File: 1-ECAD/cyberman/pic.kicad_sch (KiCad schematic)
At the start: 0 parts

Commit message: add expander io and pic
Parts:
- added C50: 100nF, symbol Device:C
- added C51: 10nF, symbol Device:C
- added R34: 100R, symbol Device:R
- added R35: 10k, symbol Device:R
- added TP5, TP6: TestPoint, symbol Connector:TestPoint
- added U19: PIC16F13115T-I/SN, symbol 0_mcu_microchip:PIC16F13115T-I/SN
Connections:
- new net: R34.1, U19.4 (RA3)
- new net: C51.1, R34.2, R35.1
- new net +3V3: C50.1, R35.2, U19.1 (VDD)
- new net GND: C50.2, C51.2, U19.8 (VSS)
- new net ICSPCLK: TP6.1, U19.6 (RA1)
- new net ICSPDAT: TP5.1, U19.7 (RA0)

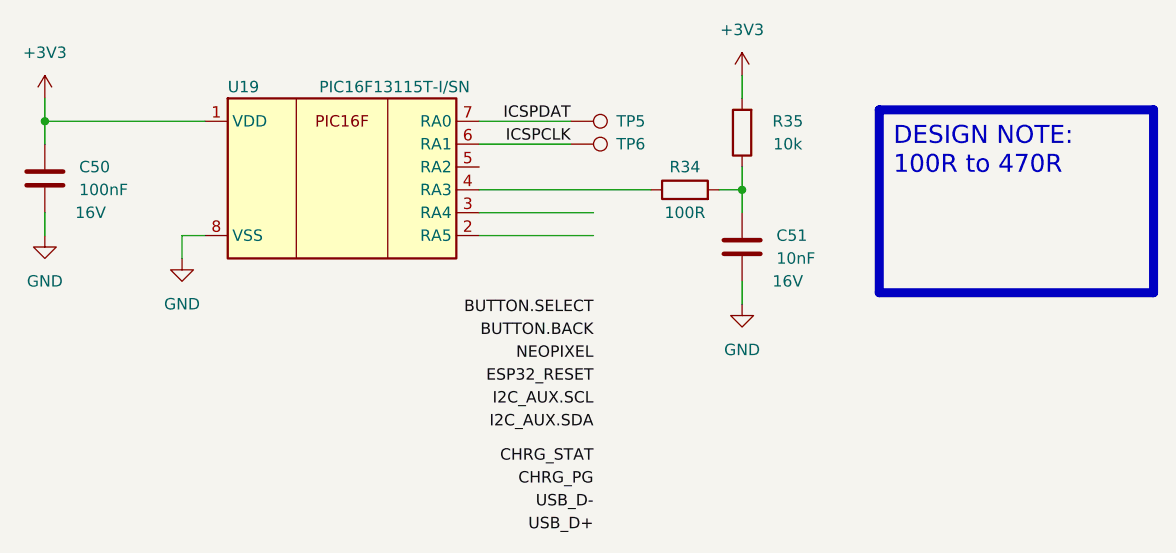
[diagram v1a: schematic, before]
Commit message: new changes
close display page and peripheral schematic
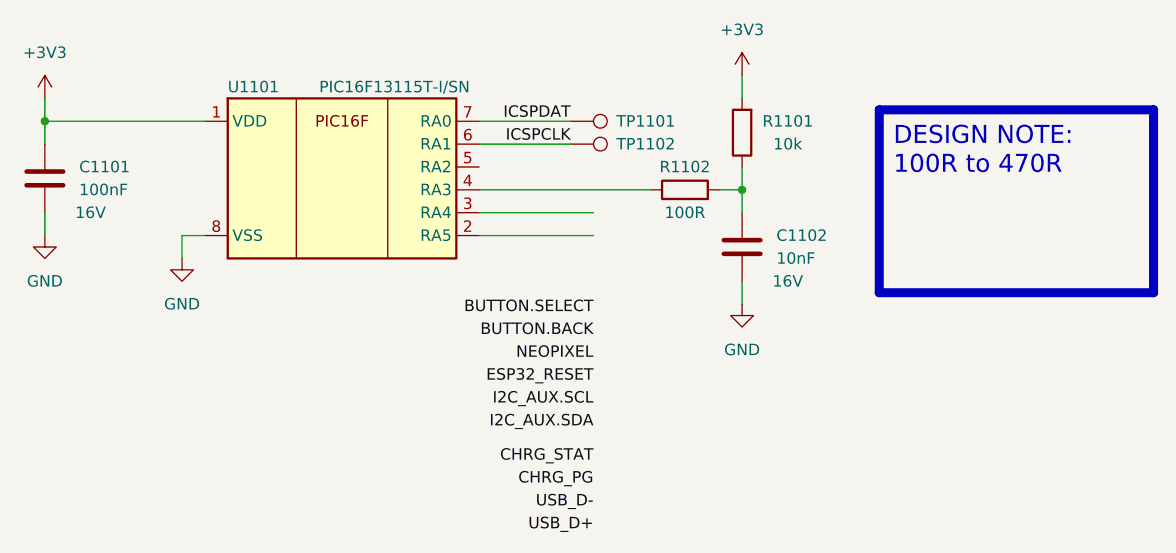
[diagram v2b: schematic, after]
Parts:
- renumbered C50 to C1101, C51 to C1102, R35 to R1101, R34 to R1102, TP5 to TP1101, TP6 to TP1102, U19 to U1101
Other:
- company: (none) -> kode.
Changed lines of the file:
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@@
 	(generator_version "8.0")
 	(paper "A4")
+	(title_block
+		(date "2024-12-11")
+		(rev "1.0")
+		(company "kode.")
+	)
 	(junction
 		(at 106.68 40.64)
@@
 		(dnp no)
 		(fields_autoplaced yes)
-		(property "Reference" "#PWR0126"
+		(property "Reference" "#PWR01105"
 			(at 184.15 67.31 0)
 			(effects
@@
 			(project "cyberman"
 				(path "/0650c7a8-acba-429c-9f8e-eec0baf0bc1c/fede4c36-00cc-4d3d-b71c-5243ba232202/9dd041dd-a789-48b0-a1c9-db40d4b09215"
-					(reference "#PWR0126")
+					(reference "#PWR01105")
 					(unit 1)
 				)
@@
 		(on_board yes)
 		(dnp no)
-		(property "Reference" "R34"
+		(property "Reference" "R1102"
 			(at 177.8 45.72 90)
 			(effects
@@
 			(project ""
 				(path "/0650c7a8-acba-429c-9f8e-eec0baf0bc1c/fede4c36-00cc-4d3d-b71c-5243ba232202/9dd041dd-a789-48b0-a1c9-db40d4b09215"
-					(reference "R34")
+					(reference "R1102")
 					(unit 1)
 				)
@@
 		(dnp no)
 		(fields_autoplaced yes)
-		(property "Reference" "#PWR0124"
+		(property "Reference" "#PWR01102"
 			(at 106.68 41.91 0)
 			(effects
@@
 			(project ""
 				(path "/0650c7a8-acba-429c-9f8e-eec0baf0bc1c/fede4c36-00cc-4d3d-b71c-5243ba232202/9dd041dd-a789-48b0-a1c9-db40d4b09215"
-					(reference "#PWR0124")
+					(reference "#PWR01102")
 					(unit 1)
 				)
@@
 		(on_board yes)
 		(dnp no)
-		(property "Reference" "TP5"
+		(property "Reference" "TP1101"
 			(at 170.18 40.64 90)
 			(effects
@@
 			(project ""
 				(path "/0650c7a8-acba-429c-9f8e-eec0baf0bc1c/fede4c36-00cc-4d3d-b71c-5243ba232202/9dd041dd-a789-48b0-a1c9-db40d4b09215"
-					(reference "TP5")
+					(reference "TP1101")
 					(unit 1)
 				)
@@
 		(dnp no)
 		(fields_autoplaced yes)
-		(property "Reference" "U19"
+		(property "Reference" "U1101"
 			(at 127 36.83 0)
 			(do_not_autoplace yes)
@@
 			(project ""
 				(path "/0650c7a8-acba-429c-9f8e-eec0baf0bc1c/fede4c36-00cc-4d3d-b71c-5243ba232202/9dd041dd-a789-48b0-a1c9-db40d4b09215"
-					(reference "U19")
+					(reference "U1101")
 					(unit 1)
 				)
@@
 		(on_board yes)
 		(dnp no)
-		(property "Reference" "C50"
+		(property "Reference" "C1101"
 			(at 110.49 45.72 0)
 			(effects
@@
 			(project ""
 				(path "/0650c7a8-acba-429c-9f8e-eec0baf0bc1c/fede4c36-00cc-4d3d-b71c-5243ba232202/9dd041dd-a789-48b0-a1c9-db40d4b09215"
-					(reference "C50")
+					(reference "C1101")
 					(unit 1)
 				)
@@
 		(dnp no)
 		(fields_autoplaced yes)
-		(property "Reference" "#PWR0122"
+		(property "Reference" "#PWR01104"
 			(at 121.92 62.23 0)
 			(effects
@@
 			(project ""
 				(path "/0650c7a8-acba-429c-9f8e-eec0baf0bc1c/fede4c36-00cc-4d3d-b71c-5243ba232202/9dd041dd-a789-48b0-a1c9-db40d4b09215"
-					(reference "#PWR0122")
+					(reference "#PWR01104")
 					(unit 1)
 				)
@@
 		(on_board yes)
 		(dnp no)
-		(property "Reference" "C51"
+		(property "Reference" "C1102"
 			(at 187.96 53.34 0)
 			(effects
@@
 			(project "cyberman"
 				(path "/0650c7a8-acba-429c-9f8e-eec0baf0bc1c/fede4c36-00cc-4d3d-b71c-5243ba232202/9dd041dd-a789-48b0-a1c9-db40d4b09215"
-					(reference "C51")
+					(reference "C1102")
 					(unit 1)
 				)
@@
 		(on_board yes)
 		(dnp no)
-		(property "Reference" "R35"
+		(property "Reference" "R1101"
 			(at 189.23 40.64 0)
 			(effects
@@
 			(project "cyberman"
 				(path "/0650c7a8-acba-429c-9f8e-eec0baf0bc1c/fede4c36-00cc-4d3d-b71c-5243ba232202/9dd041dd-a789-48b0-a1c9-db40d4b09215"
-					(reference "R35")
+					(reference "R1101")
 					(unit 1)
 				)
@@
 		(dnp no)
 		(fields_autoplaced yes)
-		(property "Reference" "#PWR0123"
+		(property "Reference" "#PWR01103"
 			(at 106.68 59.69 0)
 			(effects
@@
 			(project "cyberman"
 				(path "/0650c7a8-acba-429c-9f8e-eec0baf0bc1c/fede4c36-00cc-4d3d-b71c-5243ba232202/9dd041dd-a789-48b0-a1c9-db40d4b09215"
-					(reference "#PWR0123")
+					(reference "#PWR01103")
 					(unit 1)
 				)
@@
 		(dnp no)
 		(fields_autoplaced yes)
-		(property "Reference" "#PWR0125"
+		(property "Reference" "#PWR01101"
 			(at 184.15 39.37 0)
 			(effects
@@
 			(project "cyberman"
 				(path "/0650c7a8-acba-429c-9f8e-eec0baf0bc1c/fede4c36-00cc-4d3d-b71c-5243ba232202/9dd041dd-a789-48b0-a1c9-db40d4b09215"
-					(reference "#PWR0125")
+					(reference "#PWR01101")
 					(unit 1)
 				)
@@
 		(on_board yes)
 		(dnp no)
-		(property "Reference" "TP6"
+		(property "Reference" "TP1102"
 			(at 170.18 43.18 90)
 			(effects
@@
 			(project "cyberman"
 				(path "/0650c7a8-acba-429c-9f8e-eec0baf0bc1c/fede4c36-00cc-4d3d-b71c-5243ba232202/9dd041dd-a789-48b0-a1c9-db40d4b09215"
-					(reference "TP6")
+					(reference "TP1102")
 					(unit 1)
 				)

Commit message: power page close
siuuuuuuuuuuuu
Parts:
- C1101: value 100nF -> C; Voltage 16V -> (none)
- C1102: value 10nF -> C; Voltage 16V -> (none)
- R1101: value 10k -> R
- R1102: value 100R -> R
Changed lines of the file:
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@@
 	(paper "A4")
 	(title_block
-		(date "2024-12-11")
+		(date "2024-12-18")
 		(rev "1.0")
 		(company "kode.")
@@
 		(dnp no)
 		(fields_autoplaced yes)
-		(property "Reference" "#PWR01105"
+		(property "Reference" "#PWR1105"
 			(at 184.15 67.31 0)
 			(effects
@@
 			(project "cyberman"
 				(path "/0650c7a8-acba-429c-9f8e-eec0baf0bc1c/fede4c36-00cc-4d3d-b71c-5243ba232202/9dd041dd-a789-48b0-a1c9-db40d4b09215"
-					(reference "#PWR01105")
+					(reference "#PWR1105")
 					(unit 1)
 				)
@@
 			)
 		)
-		(property "Value" "100R"
+		(property "Value" "R"
 			(at 177.8 50.8 90)
 			(effects
@@
 		(dnp no)
 		(fields_autoplaced yes)
-		(property "Reference" "#PWR01102"
+		(property "Reference" "#PWR1102"
 			(at 106.68 41.91 0)
 			(effects
@@
 			(project ""
 				(path "/0650c7a8-acba-429c-9f8e-eec0baf0bc1c/fede4c36-00cc-4d3d-b71c-5243ba232202/9dd041dd-a789-48b0-a1c9-db40d4b09215"
-					(reference "#PWR01102")
+					(reference "#PWR1102")
 					(unit 1)
 				)
@@
 				)
 				(justify left)
-				(hide yes)
 			)
 		)
@@
 			)
 		)
-		(property "Value" "100nF"
+		(property "Value" "C"
 			(at 110.49 48.26 0)
 			(effects
@@
 				)
 				(hide yes)
-			)
-		)
-		(property "Voltage" "16V"
-			(at 111.76 50.8 0)
-			(effects
-				(font
-					(size 1.27 1.27)
-				)
 			)
 		)
@@
 		(dnp no)
 		(fields_autoplaced yes)
-		(property "Reference" "#PWR01104"
+		(property "Reference" "#PWR1104"
 			(at 121.92 62.23 0)
 			(effects
@@
 			(project ""
 				(path "/0650c7a8-acba-429c-9f8e-eec0baf0bc1c/fede4c36-00cc-4d3d-b71c-5243ba232202/9dd041dd-a789-48b0-a1c9-db40d4b09215"
-					(reference "#PWR01104")
+					(reference "#PWR1104")
 					(unit 1)
 				)
@@
 			)
 		)
-		(property "Value" "10nF"
+		(property "Value" "C"
 			(at 187.96 55.88 0)
 			(effects
@@
 				)
 				(hide yes)
-			)
-		)
-		(property "Voltage" "16V"
-			(at 189.23 58.42 0)
-			(effects
-				(font
-					(size 1.27 1.27)
-				)
 			)
 		)
@@
 			)
 		)
-		(property "Value" "10k"
+		(property "Value" "R"
 			(at 189.23 43.18 0)
 			(effects
@@
 		(dnp no)
 		(fields_autoplaced yes)
-		(property "Reference" "#PWR01103"
+		(property "Reference" "#PWR1103"
 			(at 106.68 59.69 0)
 			(effects
@@
 			(project "cyberman"
 				(path "/0650c7a8-acba-429c-9f8e-eec0baf0bc1c/fede4c36-00cc-4d3d-b71c-5243ba232202/9dd041dd-a789-48b0-a1c9-db40d4b09215"
-					(reference "#PWR01103")
+					(reference "#PWR1103")
 					(unit 1)
 				)
@@
 		(dnp no)
 		(fields_autoplaced yes)
-		(property "Reference" "#PWR01101"
+		(property "Reference" "#PWR1101"
 			(at 184.15 39.37 0)
 			(effects
@@
 			(project "cyberman"
 				(path "/0650c7a8-acba-429c-9f8e-eec0baf0bc1c/fede4c36-00cc-4d3d-b71c-5243ba232202/9dd041dd-a789-48b0-a1c9-db40d4b09215"
-					(reference "#PWR01101")
+					(reference "#PWR1101")
 					(unit 1)
 				)
@@
 				)
 				(justify left)
-				(hide yes)
-			)
-		)
+			)
+		)
